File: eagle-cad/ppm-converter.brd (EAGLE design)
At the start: 48.3 x 49.5 mm, 19 parts, among them IC1 74HC14, IC2 74HC14, U1 ATMEGA328P, Y1 16Mhz

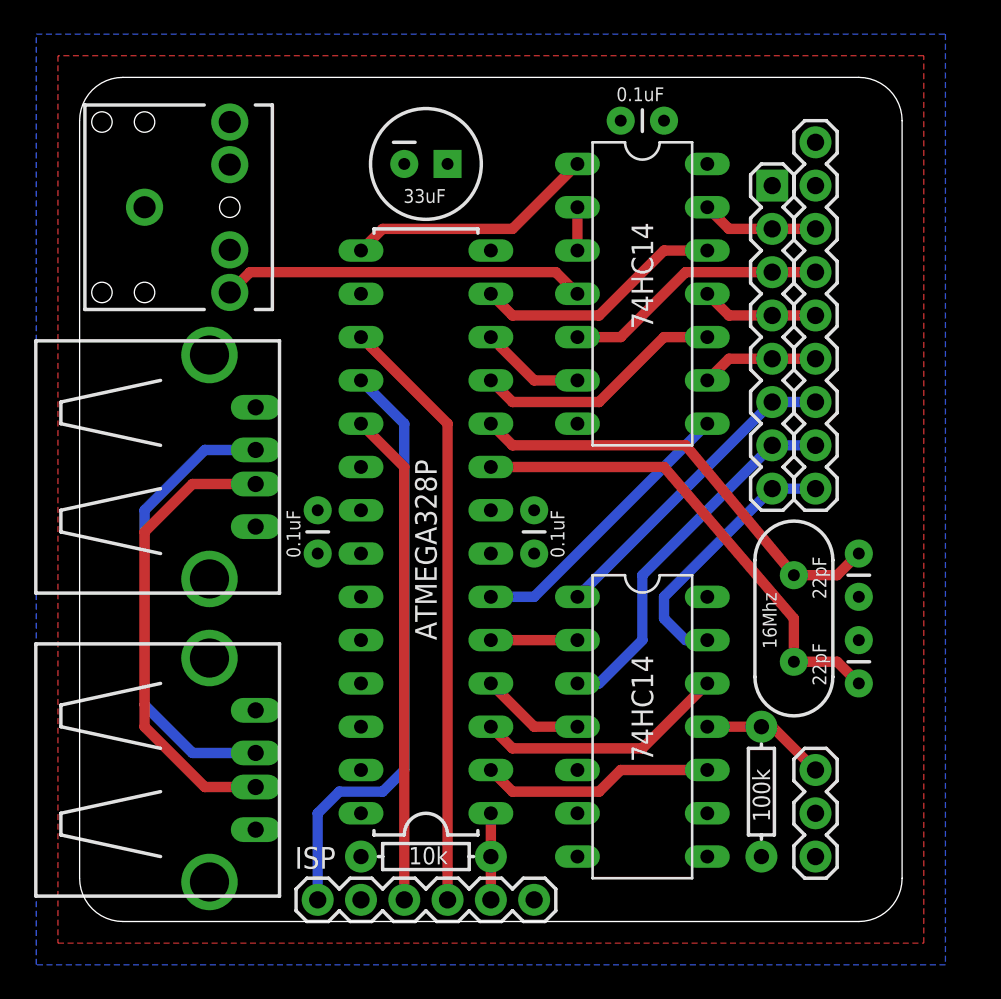
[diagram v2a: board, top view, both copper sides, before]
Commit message: Added led+resistor, finetuning some titles
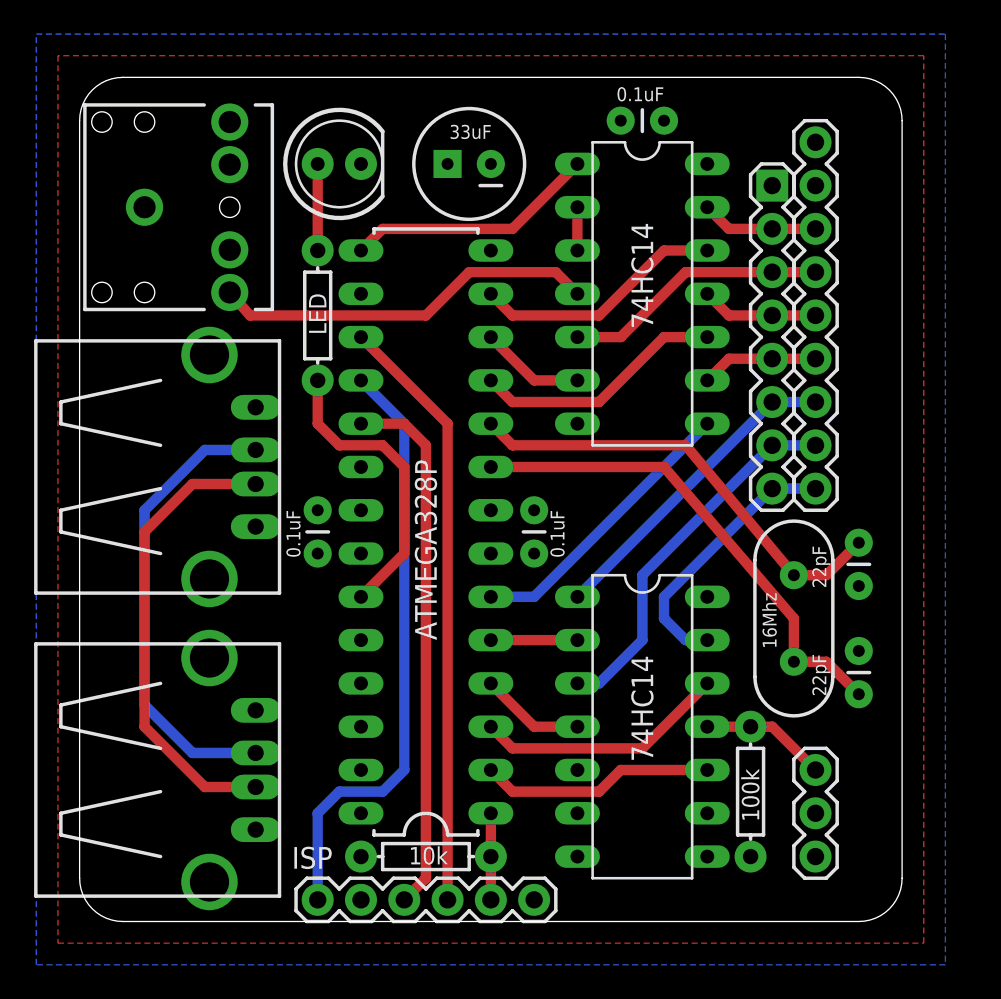
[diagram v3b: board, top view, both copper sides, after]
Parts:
- added LED: (no value), SparkFun-LED:LED5MM-KIT
- added R3: LED, SparkFun-Passives:AXIAL-0.3
- moved C7 2.54 mm to (22.9, 44.5), turned to 180 degrees
- moved R2 0.64 mm to (39.4, 7.62)
- moved C3 0.64 mm to (45.7, 22.2)
- moved C4 0.63 mm to (45.7, 13.3)
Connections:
- new net N$21: LED.A, R3.P$1
- new net N$31: R3.P$2, U1.23
- net GND: now also LED.K
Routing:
- net N$31: track 0.00 -> 17.3 mm
- net N$21: track 0.00 -> 5.08 mm
- net N$28: track 29.0 -> 31.5 mm
- net N$8: track 21.4 -> 22.6 mm
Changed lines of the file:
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@@
 <attribute name="VALUE" x="40.894" y="16.002" size="0.8128" layer="25" ratio="10" rot="R90"/>
 </element>
-<element name="C3" library="SparkFun-Passives" package="CAP-PTH-SMALL" value="22pF" x="45.72" y="21.59" smashed="yes" rot="R270">
-<attribute name="VALUE" x="43.815" y="18.923" size="0.8128" layer="25" rot="R90"/>
-</element>
-<element name="C4" library="SparkFun-Passives" package="CAP-PTH-SMALL" value="22pF" x="45.72" y="13.97" smashed="yes" rot="R90">
-<attribute name="VALUE" x="43.815" y="13.843" size="0.8128" layer="25" rot="R90"/>
+<element name="C3" library="SparkFun-Passives" package="CAP-PTH-SMALL" value="22pF" x="45.72" y="22.225" smashed="yes" rot="R270">
+<attribute name="VALUE" x="43.815" y="19.558" size="0.8128" layer="25" rot="R90"/>
+</element>
+<element name="C4" library="SparkFun-Passives" package="CAP-PTH-SMALL" value="22pF" x="45.72" y="13.335" smashed="yes" rot="R90">
+<attribute name="VALUE" x="43.815" y="13.208" size="0.8128" layer="25" rot="R90"/>
 </element>
 <element name="JP2" library="SparkFun-Connectors" package="1X03" value="" x="43.18" y="3.81" smashed="yes" rot="R90">
@@
 <attribute name="VALUE" x="31.496" y="48.133" size="0.8128" layer="25"/>
 </element>
-<element name="C7" library="SparkFun-Capacitors" package="CPOL-RADIAL-100UF-25V" value="33uF" x="20.32" y="44.45" smashed="yes">
-<attribute name="VALUE" x="18.9992" y="42.164" size="0.8128" layer="25"/>
+<element name="C7" library="SparkFun-Capacitors" package="CPOL-RADIAL-100UF-25V" value="33uF" x="22.86" y="44.45" smashed="yes" rot="R180">
+<attribute name="VALUE" x="24.1808" y="46.736" size="0.8128" layer="25" rot="R180"/>
 </element>
 <element name="JP1" library="SparkFun-Connectors" package="1X08" value="" x="40.64" y="43.18" smashed="yes" rot="R270"/>
-<element name="R2" library="SparkFun-Passives" package="AXIAL-0.3" value="100k" x="40.005" y="7.62" smashed="yes" rot="R270">
-<attribute name="VALUE" x="40.513" y="5.842" size="1.016" layer="21" font="vector" ratio="15" rot="R90"/>
-</element>
-<element name="ISP" library="SparkFun-Connectors" package="1X06" value="" x="13.97" y="1.27"/>
+<element name="R2" library="SparkFun-Passives" package="AXIAL-0.3" value="100k" x="39.37" y="7.62" smashed="yes" rot="R270">
+<attribute name="VALUE" x="39.878" y="5.842" size="1.016" layer="21" font="vector" ratio="15" rot="R90"/>
+</element>
+<element name="ISP" library="SparkFun-Connectors" package="1X06" value="" x="13.97" y="1.27" smashed="yes">
+<attribute name="NAME" x="12.446" y="3.0988" size="1.27" layer="25" ratio="10"/>
+<attribute name="VALUE" x="12.7" y="-1.905" size="1.27" layer="27"/>
+</element>
+<element name="LED" library="SparkFun-LED" package="LED5MM-KIT" value="" x="15.24" y="44.45" smashed="yes">
+<attribute name="VALUE" x="18.4404" y="42.6466" size="1.27" layer="27" ratio="10"/>
+</element>
+<element name="R3" library="SparkFun-Passives" package="AXIAL-0.3" value="LED" x="13.97" y="35.56" smashed="yes" rot="R270">
+<attribute name="VALUE" x="14.478" y="34.417" size="1.016" layer="21" font="vector" ratio="15" rot="R90"/>
+</element>
 </elements>
 <signals>
@@
 <contactref element="IC2" pad="5"/>
 <contactref element="ISP" pad="6"/>
+<contactref element="LED" pad="K"/>
 </signal>
 <signal name="N$2">
@@
 <wire x1="25.4" y1="27.94" x2="35.56" y2="27.94" width="0.6096" layer="1"/>
 <wire x1="35.56" y1="27.94" x2="41.91" y2="20.32" width="0.6096" layer="1"/>
-<wire x1="41.91" y1="20.32" x2="44.45" y2="20.32" width="0.6096" layer="1"/>
 <wire x1="25.4" y1="27.94" x2="24.13" y2="29.21" width="0.6096" layer="1"/>
-<wire x1="44.45" y1="20.32" x2="45.72" y2="21.59" width="0.6096" layer="1"/>
+<wire x1="41.91" y1="20.32" x2="43.815" y2="20.32" width="0.6096" layer="1"/>
+<wire x1="43.815" y1="20.32" x2="45.72" y2="22.225" width="0.6096" layer="1"/>
 </signal>
 <signal name="N$6">
@@
 <wire x1="34.29" y1="26.67" x2="41.91" y2="17.78" width="0.6096" layer="1"/>
 <wire x1="41.91" y1="17.78" x2="41.91" y2="15.24" width="0.6096" layer="1"/>
-<wire x1="41.91" y1="15.24" x2="44.45" y2="15.24" width="0.6096" layer="1"/>
-<wire x1="44.45" y1="15.24" x2="45.72" y2="13.97" width="0.6096" layer="1"/>
+<wire x1="41.91" y1="15.24" x2="43.815" y2="15.24" width="0.6096" layer="1"/>
+<wire x1="43.815" y1="15.24" x2="45.72" y2="13.335" width="0.6096" layer="1"/>
 </signal>
 <signal name="N$9">
@@
 <contactref element="R2" pad="P$1"/>
 <contactref element="IC2" pad="11"/>
-<wire x1="40.005" y1="11.43" x2="36.83" y2="11.43" width="0.6096" layer="1"/>
-<wire x1="40.005" y1="11.43" x2="40.64" y2="11.43" width="0.6096" layer="1"/>
+<wire x1="39.37" y1="11.43" x2="36.83" y2="11.43" width="0.6096" layer="1"/>
+<wire x1="39.37" y1="11.43" x2="40.64" y2="11.43" width="0.6096" layer="1"/>
 <wire x1="40.64" y1="11.43" x2="43.18" y2="8.89" width="0.6096" layer="1"/>
 </signal>
@@
 <contactref element="U2" pad="TIP"/>
 <wire x1="29.21" y1="36.83" x2="27.94" y2="38.1" width="0.6096" layer="1"/>
-<wire x1="27.94" y1="38.1" x2="10" y2="38.1" width="0.6096" layer="1"/>
-<wire x1="10" y1="38.1" x2="8.81" y2="36.91" width="0.6096" layer="1"/>
+<wire x1="27.94" y1="38.1" x2="22.86" y2="38.1" width="0.6096" layer="1"/>
+<wire x1="22.86" y1="38.1" x2="20.32" y2="35.56" width="0.6096" layer="1"/>
+<wire x1="20.32" y1="35.56" x2="10" y2="35.56" width="0.6096" layer="1"/>
+<wire x1="10" y1="35.56" x2="8.81" y2="36.91" width="0.6096" layer="1"/>
 </signal>
 <signal name="N$17">
@@
 <contactref element="U1" pad="19"/>
 <contactref element="ISP" pad="3"/>
-<wire x1="19.05" y1="1.27" x2="19.05" y2="26.67" width="0.6096" layer="1"/>
-<wire x1="19.05" y1="26.67" x2="16.51" y2="29.21" width="0.6096" layer="1"/>
+<wire x1="19.05" y1="1.27" x2="20.32" y2="2.54" width="0.6096" layer="1"/>
+<wire x1="20.32" y1="2.54" x2="20.32" y2="27.94" width="0.6096" layer="1"/>
+<wire x1="20.32" y1="27.94" x2="19.05" y2="29.21" width="0.6096" layer="1"/>
+<wire x1="19.05" y1="29.21" x2="16.51" y2="29.21" width="0.6096" layer="1"/>
 </signal>
 <signal name="N$29">
@@
 <wire x1="21.59" y1="29.21" x2="16.51" y2="34.29" width="0.6096" layer="1"/>
 </signal>
+<signal name="N$21">
+<contactref element="R3" pad="P$1"/>
+<contactref element="LED" pad="A"/>
+<wire x1="13.97" y1="39.37" x2="13.97" y2="44.45" width="0.6096" layer="1"/>
+</signal>
+<signal name="N$31">
+<contactref element="U1" pad="23"/>
+<contactref element="R3" pad="P$2"/>
+<wire x1="15.24" y1="27.94" x2="17.78" y2="27.94" width="0.6096" layer="1"/>
+<wire x1="17.78" y1="27.94" x2="19.05" y2="26.67" width="0.6096" layer="1"/>
+<wire x1="19.05" y1="26.67" x2="19.05" y2="21.59" width="0.6096" layer="1"/>
+<wire x1="19.05" y1="21.59" x2="16.51" y2="19.05" width="0.6096" layer="1"/>
+<wire x1="13.97" y1="31.75" x2="13.97" y2="29.21" width="0.6096" layer="1"/>
+<wire x1="13.97" y1="29.21" x2="15.24" y2="27.94" width="0.6096" layer="1"/>
+</signal>
 </signals>

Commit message: Changed version -> revision, added 0.1uF cap
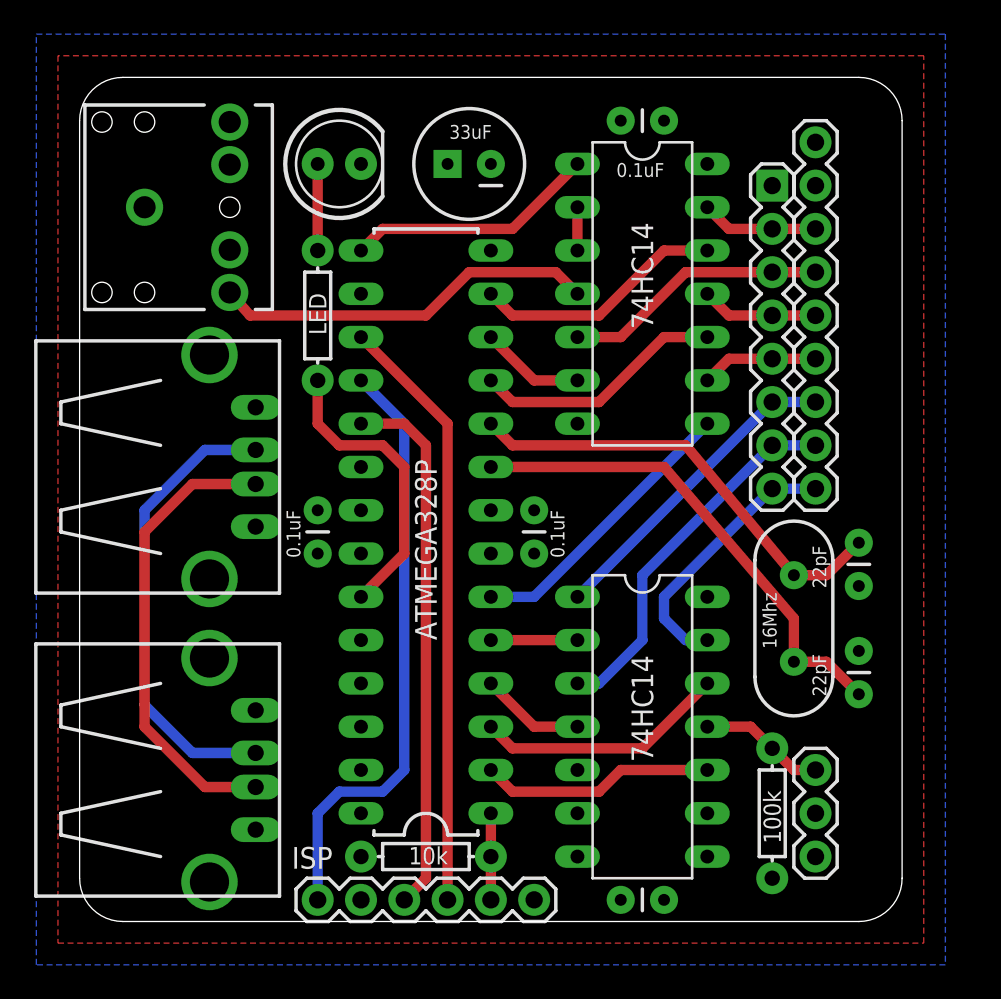
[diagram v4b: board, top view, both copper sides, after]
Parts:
- added C5: 0.1uF, SparkFun-Passives:CAP-PTH-SMALL
- moved R2 1.80 mm to (40.6, 6.35)
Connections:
- net GND: now also C5.2
- net VCC: now also C5.1
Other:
- board text added: "r02"
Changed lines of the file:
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@@
 <wire x1="48.26" y1="2.54" x2="45.72" y2="0" width="0" layer="20" curve="-90"/>
 <wire x1="2.54" y1="0" x2="0" y2="2.54" width="0" layer="20" curve="-90"/>
+<text x="29.21" y="21.971" size="1.778" layer="26" rot="MR90">r02</text>
 </plain>
 <attributes>
@@
 <element name="JP3" library="SparkFun-Connectors" package="1X09" value="M09" x="43.18" y="45.72" smashed="yes" rot="R270"/>
 <element name="C6" library="SparkFun-Passives" package="CAP-PTH-SMALL" value="0.1uF" x="34.29" y="46.99" smashed="yes" rot="R180">
-<attribute name="VALUE" x="31.496" y="48.133" size="0.8128" layer="25"/>
+<attribute name="VALUE" x="31.496" y="43.688" size="0.8128" layer="25"/>
 </element>
 <element name="C7" library="SparkFun-Capacitors" package="CPOL-RADIAL-100UF-25V" value="33uF" x="22.86" y="44.45" smashed="yes" rot="R180">
@@
 </element>
 <element name="JP1" library="SparkFun-Connectors" package="1X08" value="" x="40.64" y="43.18" smashed="yes" rot="R270"/>
-<element name="R2" library="SparkFun-Passives" package="AXIAL-0.3" value="100k" x="39.37" y="7.62" smashed="yes" rot="R270">
-<attribute name="VALUE" x="39.878" y="5.842" size="1.016" layer="21" font="vector" ratio="15" rot="R90"/>
+<element name="R2" library="SparkFun-Passives" package="AXIAL-0.3" value="100k" x="40.64" y="6.35" smashed="yes" rot="R270">
+<attribute name="VALUE" x="41.148" y="4.572" size="1.016" layer="21" font="vector" ratio="15" rot="R90"/>
 </element>
 <element name="ISP" library="SparkFun-Connectors" package="1X06" value="" x="13.97" y="1.27" smashed="yes">
@@
 <element name="R3" library="SparkFun-Passives" package="AXIAL-0.3" value="LED" x="13.97" y="35.56" smashed="yes" rot="R270">
 <attribute name="VALUE" x="14.478" y="34.417" size="1.016" layer="21" font="vector" ratio="15" rot="R90"/>
+</element>
+<element name="C5" library="SparkFun-Passives" package="CAP-PTH-SMALL" value="0.1uF" x="34.29" y="1.27" smashed="yes" rot="R180">
+<attribute name="VALUE" x="31.496" y="2.794" size="0.8128" layer="27"/>
 </element>
 </elements>
@@
 <contactref element="ISP" pad="6"/>
 <contactref element="LED" pad="K"/>
+<contactref element="C5" pad="2"/>
 </signal>
 <signal name="N$2">
@@
 <contactref element="R2" pad="P$1"/>
 <contactref element="IC2" pad="11"/>
-<wire x1="39.37" y1="11.43" x2="36.83" y2="11.43" width="0.6096" layer="1"/>
-<wire x1="39.37" y1="11.43" x2="40.64" y2="11.43" width="0.6096" layer="1"/>
-<wire x1="40.64" y1="11.43" x2="43.18" y2="8.89" width="0.6096" layer="1"/>
+<wire x1="36.83" y1="11.43" x2="39.37" y2="11.43" width="0.6096" layer="1"/>
+<wire x1="39.37" y1="11.43" x2="40.64" y2="10.16" width="0.6096" layer="1"/>
+<wire x1="43.18" y1="8.89" x2="41.91" y2="8.89" width="0.6096" layer="1"/>
+<wire x1="41.91" y1="8.89" x2="40.64" y2="10.16" width="0.6096" layer="1"/>
 </signal>
 <signal name="N$26">
@@
 <contactref element="IC2" pad="14"/>
 <contactref element="ISP" pad="2"/>
+<contactref element="C5" pad="1"/>
 </signal>
 <signal name="N$1">
